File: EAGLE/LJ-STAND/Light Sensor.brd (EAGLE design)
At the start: 119 x 119 mm, 122 parts

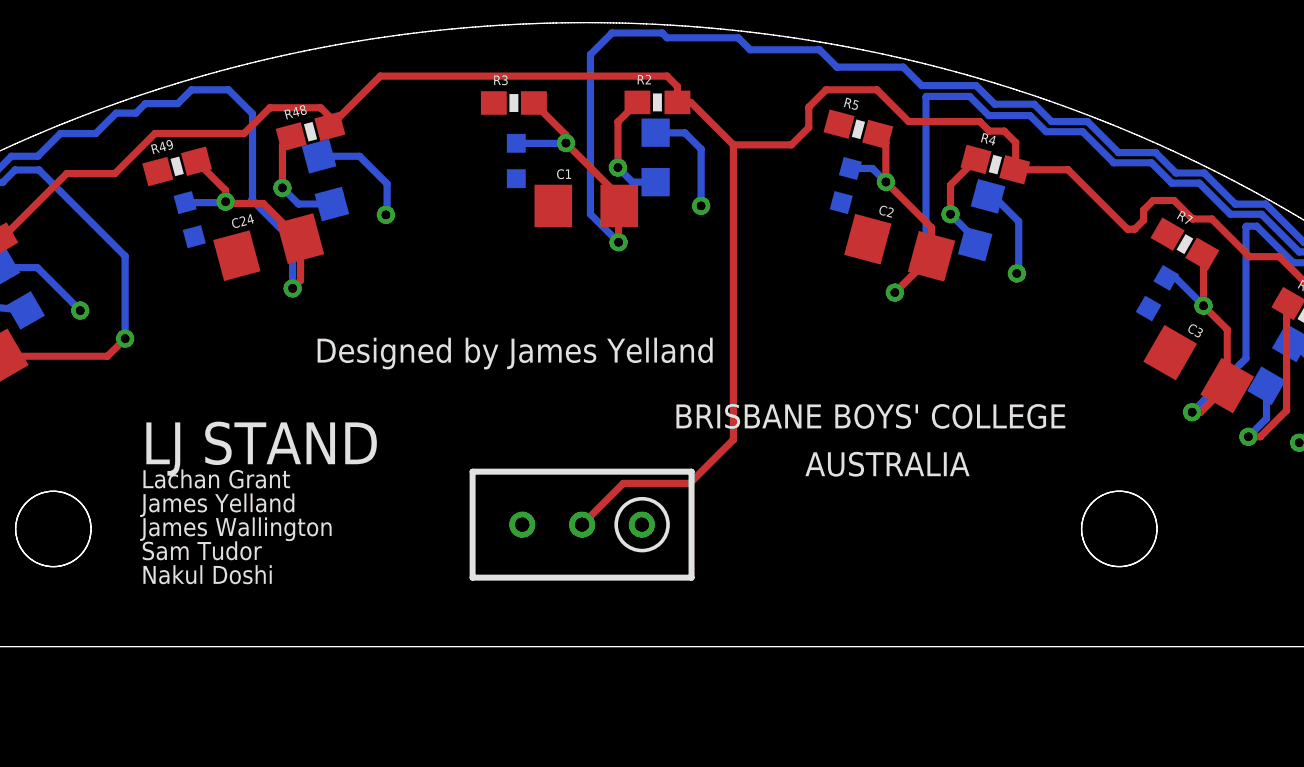
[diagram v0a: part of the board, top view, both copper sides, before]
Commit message: Logo on light pcb
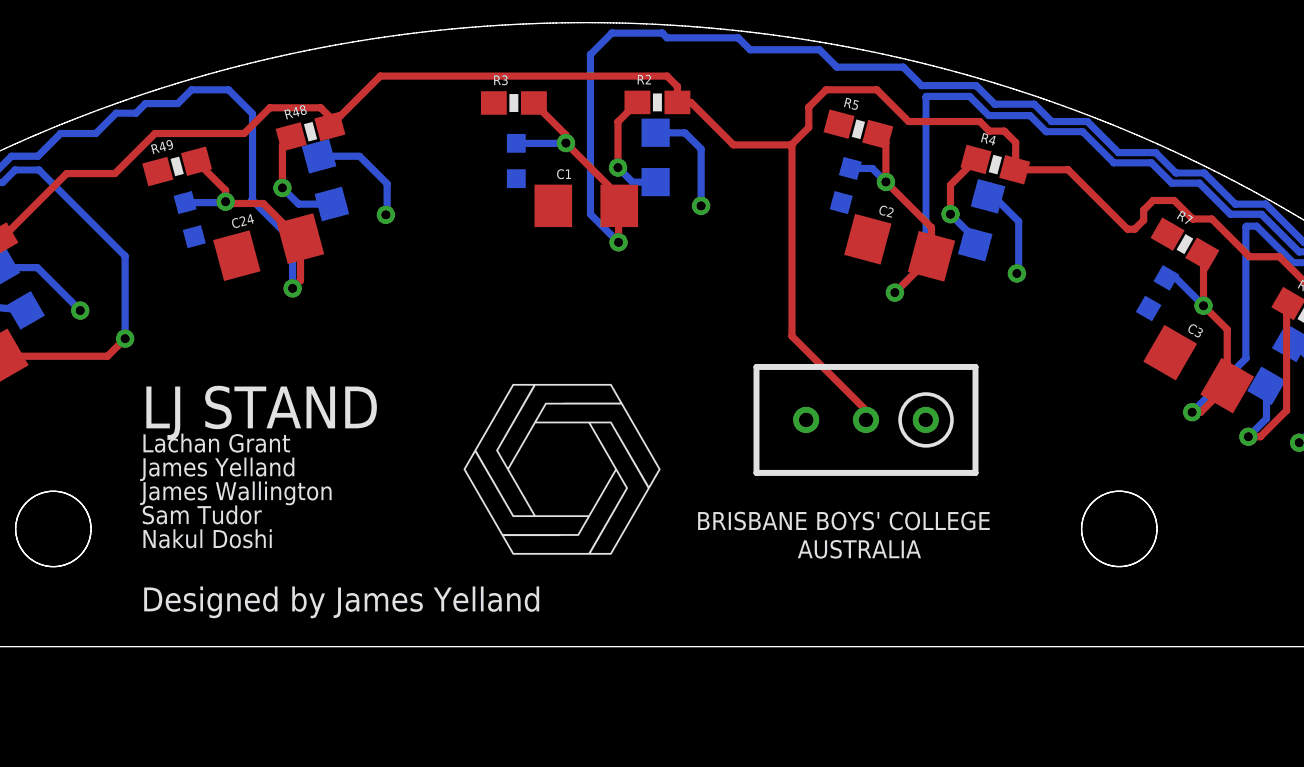
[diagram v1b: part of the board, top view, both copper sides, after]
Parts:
- moved R1 12.9 mm to (160.6, 147.9)
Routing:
- net LED_PWR: track 407.7 -> 400.3 mm

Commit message: Main pcb
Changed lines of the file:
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@@
 <rectangle x1="145.561053125" y1="149.44725" x2="149.767290625" y2="149.45486875" layer="21"/>
 <rectangle x1="145.568671875" y1="149.454871875" x2="149.759671875" y2="149.462490625" layer="21"/>
+<wire x1="146.2024" y1="69.5706" x2="151.4856" y2="69.5706" width="0.4064" layer="21"/>
 </plain>
 <attributes>

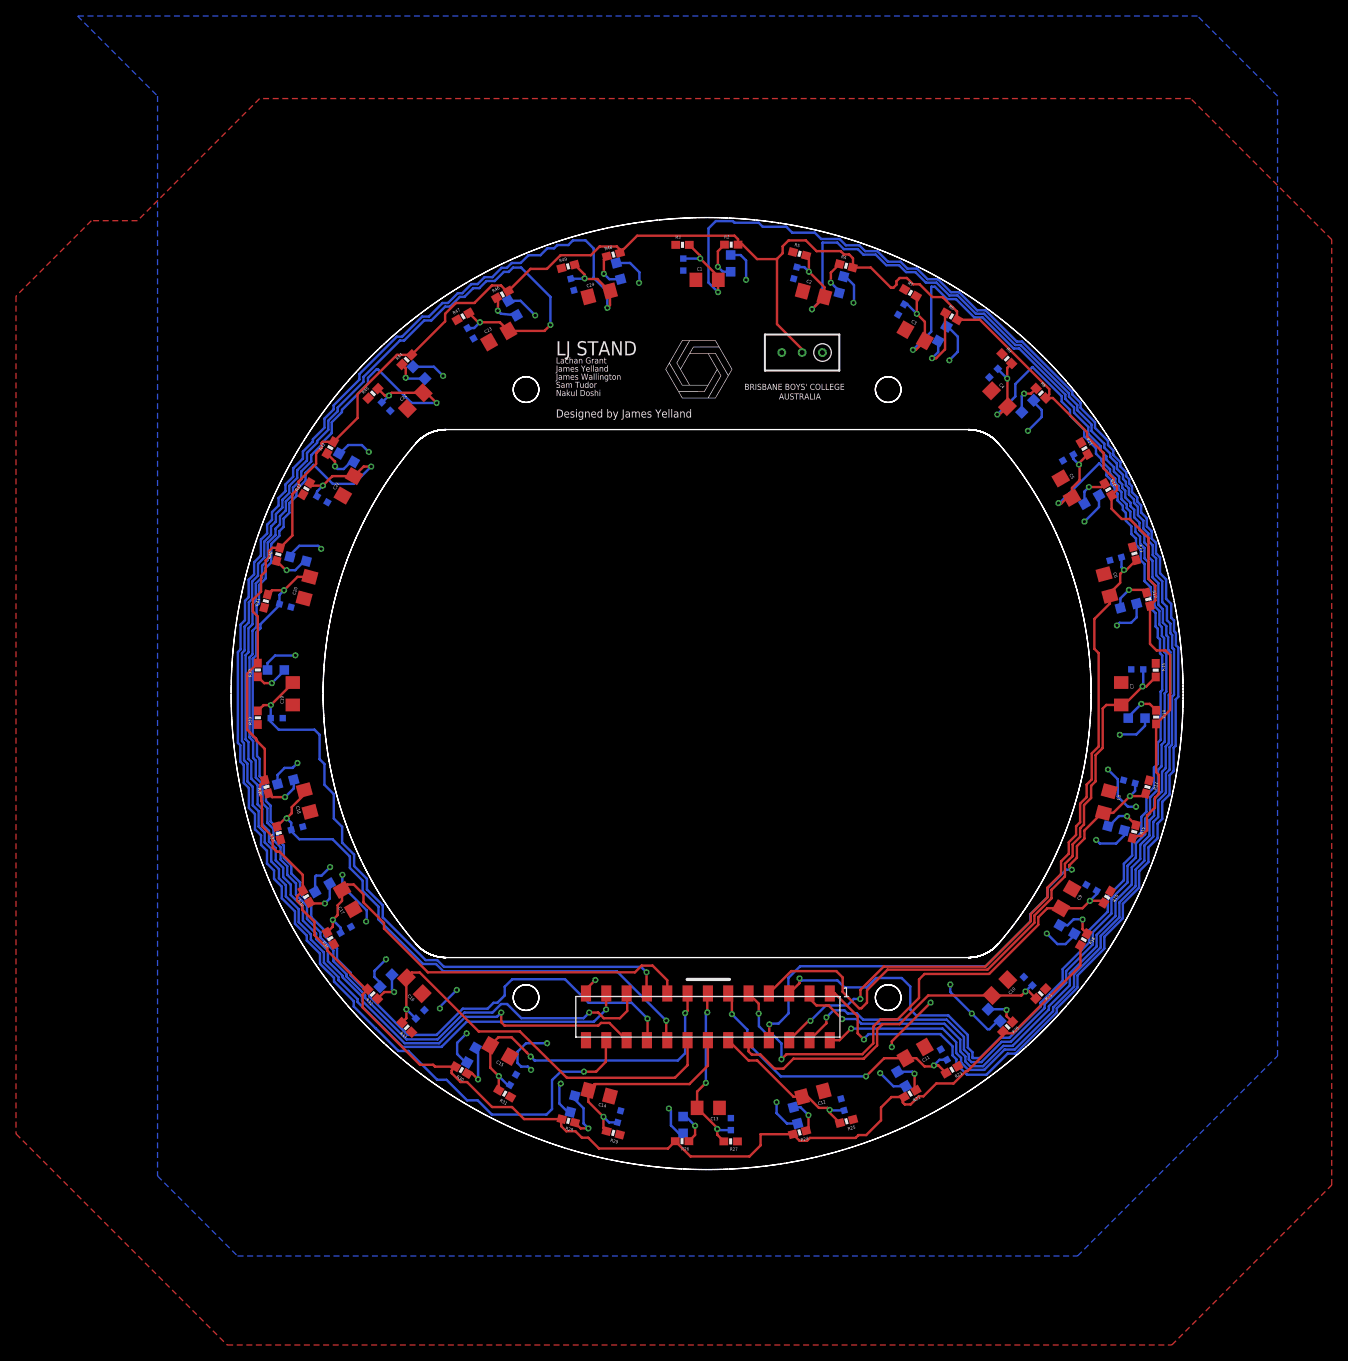
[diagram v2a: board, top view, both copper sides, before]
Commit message: Light sensor PCB error fixing
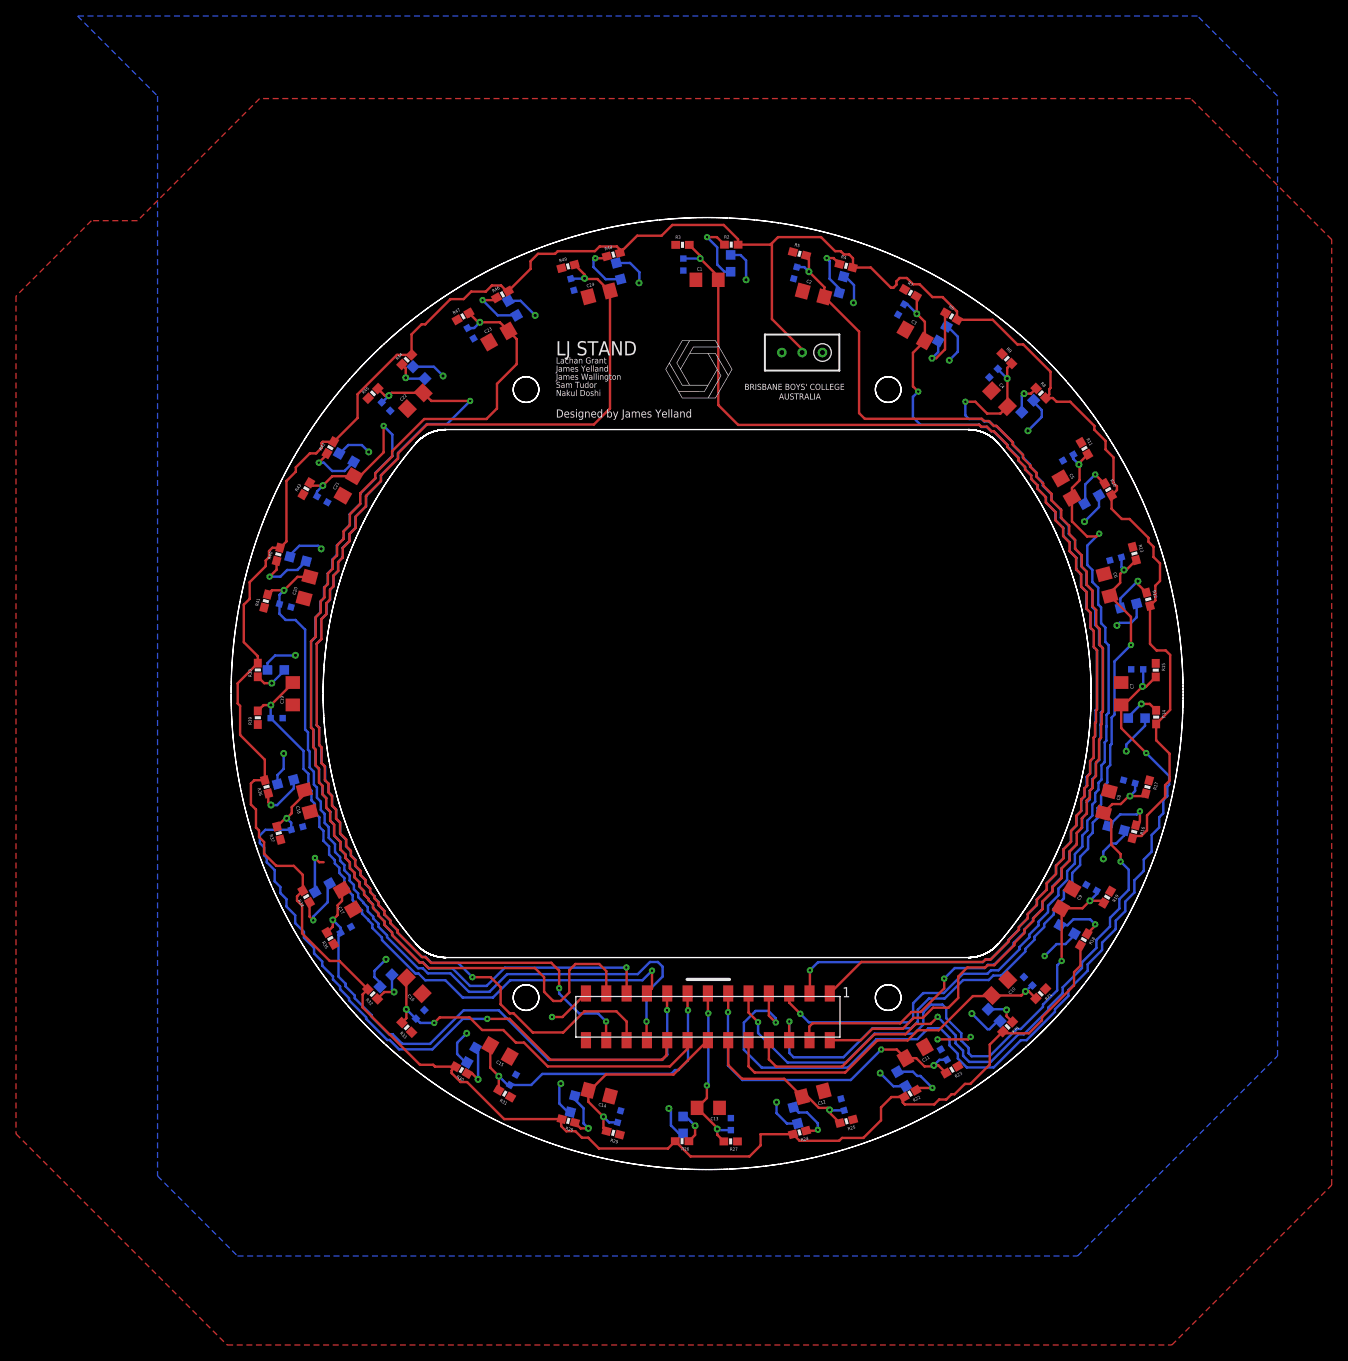
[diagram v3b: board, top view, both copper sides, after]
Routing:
- net LS0: track 200.8 -> 158.2 mm, vias 3 -> 1
- net LS23: track 190.8 -> 154.3 mm
- net LS2: track 168.1 -> 132.6 mm
- net LS1: track 181.3 -> 146.6 mm, vias 3 -> 1
- net LS22: track 175.5 -> 141.5 mm, vias 3 -> 1
- net LS6: track 83.4 -> 115.3 mm, vias 1 -> 3
- net LS4: track 137.8 -> 109.2 mm
- net GND: track 137.3 -> 110.3 mm, vias 33 -> 24
- net LS3: track 148.3 -> 126.9 mm
- net LS21: track 149.9 -> 132.8 mm
- net LED_PWR: track 400.3 -> 416.4 mm
- net LS17: track 69.6 -> 85.4 mm
- net LS7: track 68.9 -> 84.5 mm
- net LS16: track 57.4 -> 71.1 mm, vias 1 -> 2
- net LS20: track 136.8 -> 124.7 mm
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
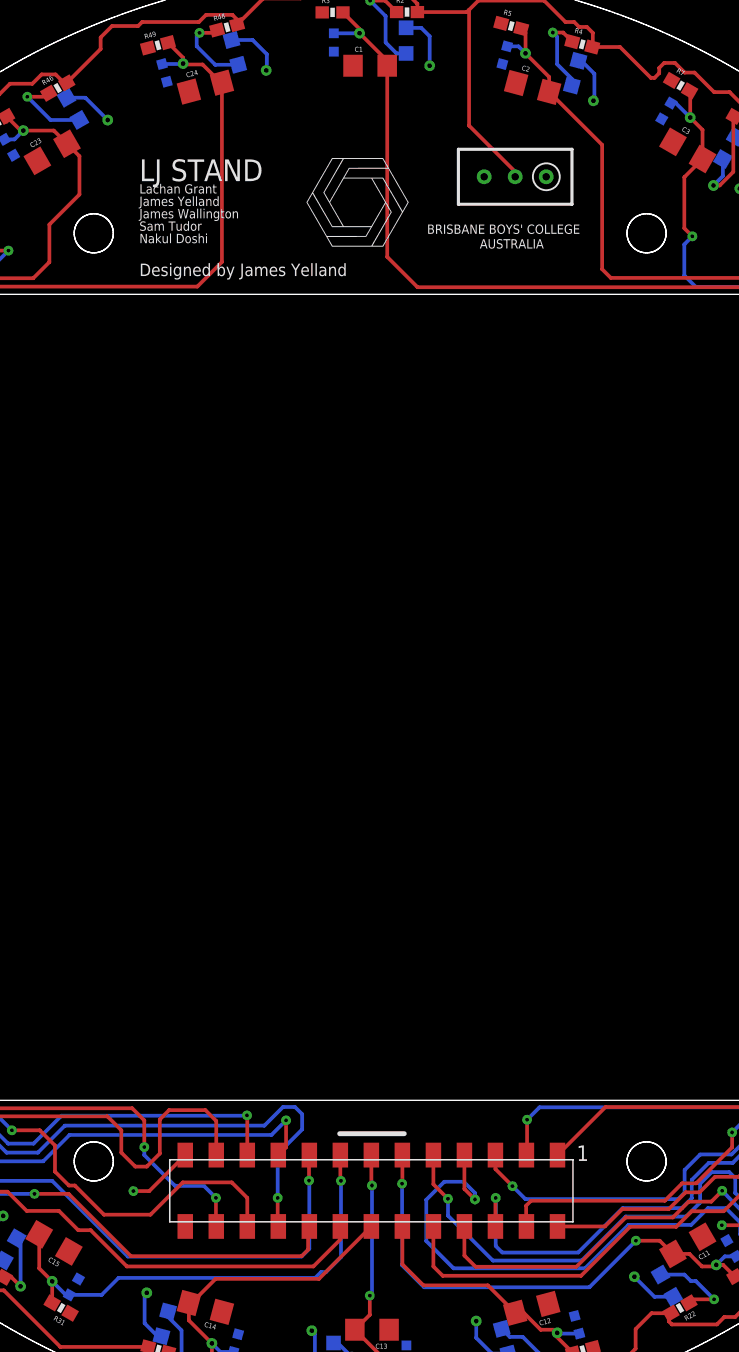
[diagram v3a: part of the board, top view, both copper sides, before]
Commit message: Main pcb check against dimensions, made text bigger on both pcbs
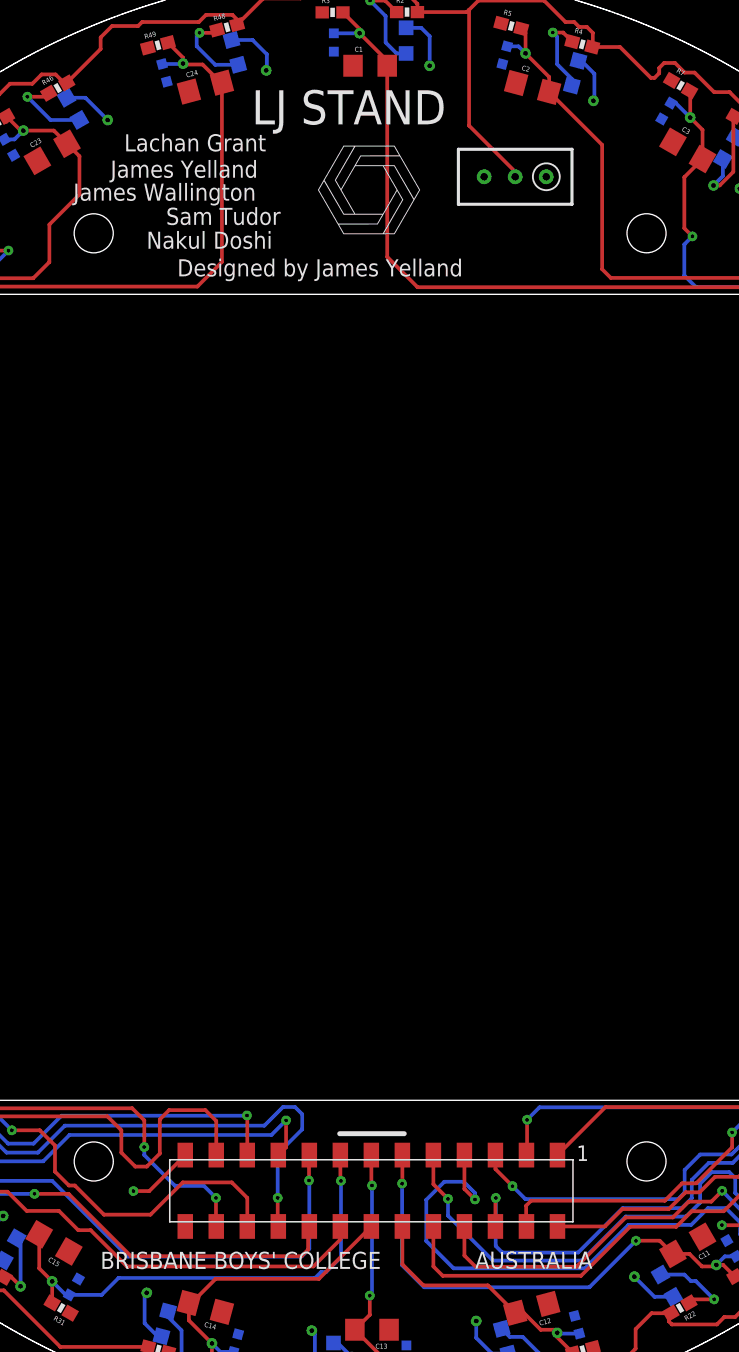
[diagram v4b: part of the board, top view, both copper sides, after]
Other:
- outline, holes or cut-outs redrawn
